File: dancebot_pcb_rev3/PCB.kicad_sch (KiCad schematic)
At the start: 30 parts, among them J1 Voltage Regulator, J10 NeoPixel Right Eye, J11 Rocker Switch, J2 IO14 servo 1, J3 IO13 servo 2, J4 IO12 servo 3, J5 IO15 servo 4, J6 IO18 servo 5 (hat), J8 Pins, J9 NeoPixel Left Eye, Q1 IRLML6402TRPBF, U1 IRLML2502TRPBF, U2 ESP32-DEVKITC-32U

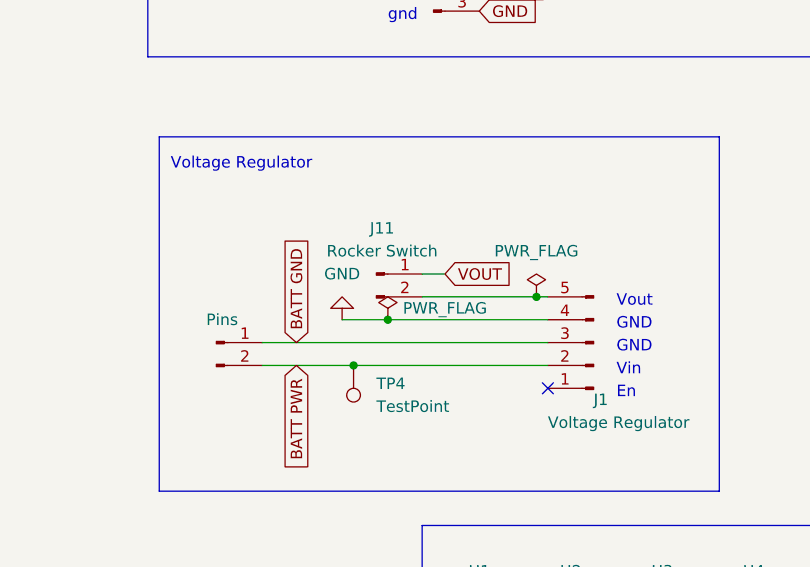
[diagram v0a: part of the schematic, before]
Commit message: changed BATT GND to GND, added some silkscreen labels
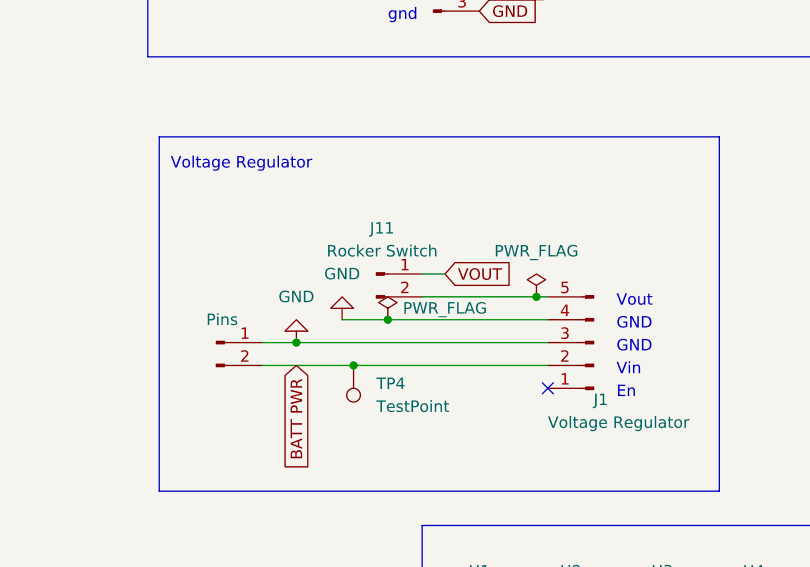
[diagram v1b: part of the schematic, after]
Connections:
- net BATT GND is gone; now on net GND: J1.3 (Pin_3), J8.1 (Pin_1)
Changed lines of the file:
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@@
   (junction (at 195.58 91.44) (diameter 0) (color 0 0 0 0)
+  )
+  (junction (at 96.52 121.92) (diameter 0) (color 0 0 0 0)
   )
   (junction (at 123.19 116.84) (diameter 0) (color 0 0 0 0)
@@
     (stroke (width 0) (type default))
   )
-  (wire (pts (xy 92.71 121.92) (xy 124.46 121.92))
+  (wire (pts (xy 92.71 121.92) (xy 96.52 121.92))
     (stroke (width 0) (type default))
   )
@@
   )
   (wire (pts (xy 101.6 119.38) (xy 106.68 119.38))
+    (stroke (width 0) (type default))
+  )
+  (wire (pts (xy 96.52 121.92) (xy 124.46 121.92))
     (stroke (width 0) (type default))
   )
@@
     (effects (font (size 1.27 1.27)) (justify left))
     (property "Intersheetrefs" "${INTERSHEET_REFS}" (at 231.948 25.4 0)
-      (effects (font (size 1.27 1.27)) (justify left) hide)
-    )
-  )
-  (global_label "BATT GND" (shape input) (at 96.52 121.92 90) (fields_autoplaced)
-    (effects (font (size 1.27 1.27)) (justify left))
-    (property "Intersheetrefs" "${INTERSHEET_REFS}" (at 96.52 109.8029 90)
       (effects (font (size 1.27 1.27)) (justify left) hide)
     )
@@
         )
       )
+    )
+  )
+  (symbol (lib_id "power:GND") (at 96.52 121.92 180) (unit 1)
+    (in_bom yes) (on_board yes) (dnp no) (fields_autoplaced)
+    (property "Reference" "#PWR04" (at 96.52 115.57 0)
+      (effects (font (size 1.27 1.27)) hide)
+    )
+    (property "Value" "GND" (at 96.52 116.84 0)
+      (effects (font (size 1.27 1.27)))
+    )
+    (property "Footprint" "" (at 96.52 121.92 0)
+      (effects (font (size 1.27 1.27)) hide)
+    )
+    (property "Datasheet" "" (at 96.52 121.92 0)
+      (effects (font (size 1.27 1.27)) hide)
+    )
+    (pin "1")
+    (instances
+      (project "PCB"
+        (path "/21324b60-e5e7-4de6-a38d-f4cdf81a1b2c"
+          (reference "#PWR04") (unit 1)
+        )
+      )

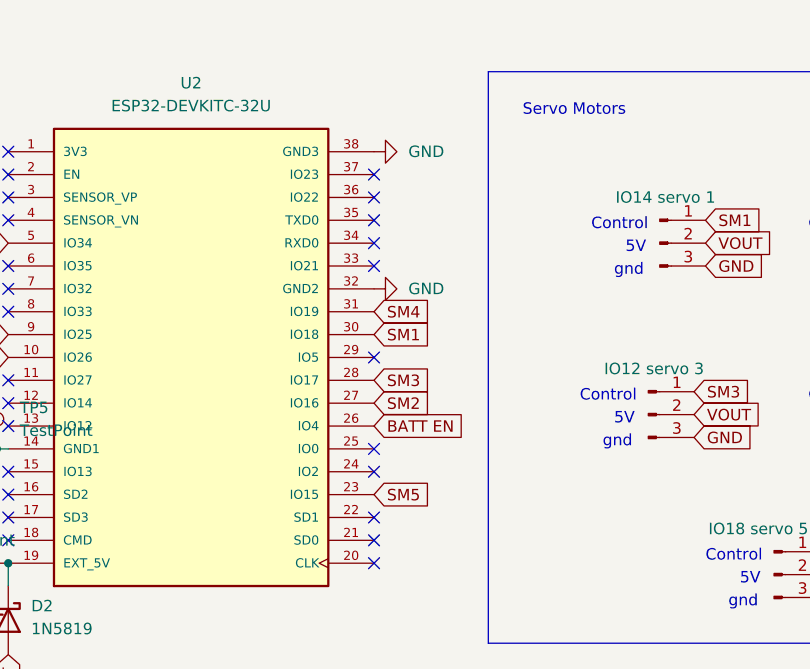
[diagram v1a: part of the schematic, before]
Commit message: shifted servo control pins to not occupy gpio15, a pin used during bootup
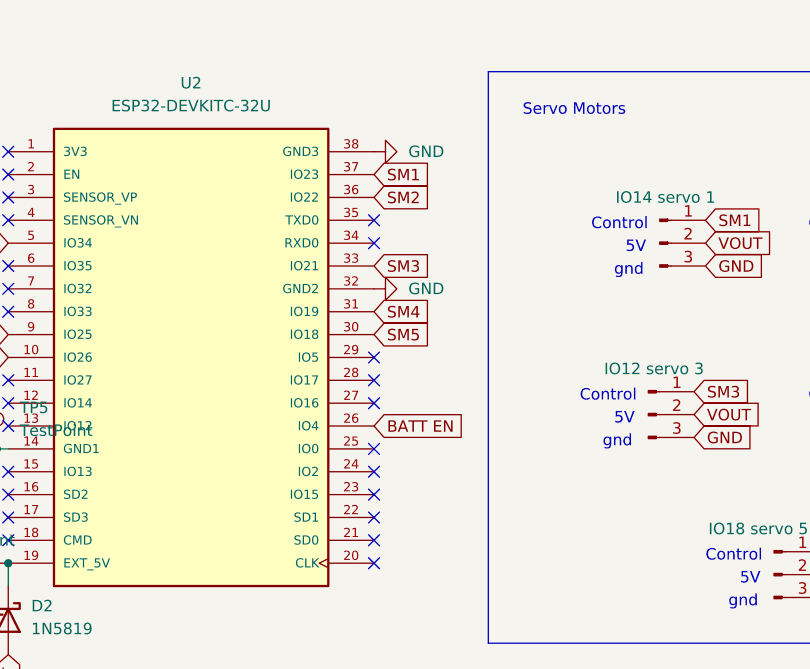
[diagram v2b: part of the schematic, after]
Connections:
- net SM1: now also U2.37 (IO23); no longer U2.30 (IO18)
- net SM2: now also U2.36 (IO22); no longer U2.27 (IO16)
- net SM3: now also U2.33 (IO21); no longer U2.28 (IO17)
- net SM5: now also U2.30 (IO18); no longer U2.23 (IO15)
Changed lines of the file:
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@@
   )
   (no_connect (at 67.31 58.42))
-  (no_connect (at 67.31 48.26))
   (no_connect (at 26.67 71.12))
   (no_connect (at 26.67 38.1))
   (no_connect (at 26.67 48.26))
   (no_connect (at 67.31 76.2))
-  (no_connect (at 67.31 38.1))
-  (no_connect (at 67.31 40.64))
   (no_connect (at 26.67 43.18))
   (no_connect (at 26.67 78.74))
@@
   (no_connect (at 170.18 129.54))
   (no_connect (at 26.67 66.04))
+  (no_connect (at 67.31 60.96))
   (no_connect (at 124.46 127))
   (no_connect (at 26.67 73.66))
+  (no_connect (at 67.31 73.66))
+  (no_connect (at 67.31 63.5))
   (no_connect (at 26.67 50.8))
   (no_connect (at 67.31 78.74))
@@
     )
   )
-  (global_label "SM3" (shape input) (at 67.31 60.96 0) (fields_autoplaced)
-    (effects (font (size 1.27 1.27)) (justify left))
-    (property "Intersheetrefs" "${INTERSHEET_REFS}" (at 74.1656 60.96 0)
-      (effects (font (size 1.27 1.27)) (justify left) hide)
-    )
-  )
   (global_label "NPLeftEye" (shape input) (at 170.18 121.92 0) (fields_autoplaced)
     (effects (font (size 1.27 1.27)) (justify left))
@@
     )
   )
+  (global_label "SM4" (shape input) (at 67.31 53.34 0) (fields_autoplaced)
+    (effects (font (size 1.27 1.27)) (justify left))
+    (property "Intersheetrefs" "${INTERSHEET_REFS}" (at 74.1656 53.34 0)
+      (effects (font (size 1.27 1.27)) (justify left) hide)
+    )
+  )
   (global_label "SM3" (shape input) (at 102.87 62.23 0) (fields_autoplaced)
     (effects (font (size 1.27 1.27)) (justify left))
@@
     )
   )
-  (global_label "SM2" (shape input) (at 67.31 63.5 0) (fields_autoplaced)
-    (effects (font (size 1.27 1.27)) (justify left))
-    (property "Intersheetrefs" "${INTERSHEET_REFS}" (at 74.1656 63.5 0)
-      (effects (font (size 1.27 1.27)) (justify left) hide)
-    )
-  )
   (global_label "VOUT" (shape input) (at 113.03 114.3 0) (fields_autoplaced)
     (effects (font (size 1.27 1.27)) (justify left))
@@
     )
   )
+  (global_label "SM3" (shape input) (at 67.31 48.26 0) (fields_autoplaced)
+    (effects (font (size 1.27 1.27)) (justify left))
+    (property "Intersheetrefs" "${INTERSHEET_REFS}" (at 74.1656 48.26 0)
+      (effects (font (size 1.27 1.27)) (justify left) hide)
+    )
+  )
   (global_label "NPLeftEye" (shape input) (at 26.67 55.88 180) (fields_autoplaced)
     (effects (font (size 1.27 1.27)) (justify right))
@@
     )
   )
-  (global_label "SM5" (shape input) (at 67.31 73.66 0) (fields_autoplaced)
-    (effects (font (size 1.27 1.27)) (justify left))
-    (property "Intersheetrefs" "${INTERSHEET_REFS}" (at 74.1656 73.66 0)
+  (global_label "SM2" (shape input) (at 67.31 40.64 0) (fields_autoplaced)
+    (effects (font (size 1.27 1.27)) (justify left))
+    (property "Intersheetrefs" "${INTERSHEET_REFS}" (at 74.1656 40.64 0)
       (effects (font (size 1.27 1.27)) (justify left) hide)
     )
@@
     )
   )
-  (global_label "SM1" (shape input) (at 67.31 55.88 0) (fields_autoplaced)
+  (global_label "SM1" (shape input) (at 67.31 38.1 0) (fields_autoplaced)
+    (effects (font (size 1.27 1.27)) (justify left))
+    (property "Intersheetrefs" "${INTERSHEET_REFS}" (at 74.1656 38.1 0)
+      (effects (font (size 1.27 1.27)) (justify left) hide)
+    )
+  )
+  (global_label "GND" (shape input) (at 128.27 48.26 0) (fields_autoplaced)
+    (effects (font (size 1.27 1.27)) (justify left))
+    (property "Intersheetrefs" "${INTERSHEET_REFS}" (at 135.1257 48.26 0)
+      (effects (font (size 1.27 1.27)) (justify left) hide)
+    )
+  )
+  (global_label "SM5" (shape input) (at 67.31 55.88 0) (fields_autoplaced)
     (effects (font (size 1.27 1.27)) (justify left))
     (property "Intersheetrefs" "${INTERSHEET_REFS}" (at 74.1656 55.88 0)
@@
     )
   )
-  (global_label "GND" (shape input) (at 128.27 48.26 0) (fields_autoplaced)
-    (effects (font (size 1.27 1.27)) (justify left))
-    (property "Intersheetrefs" "${INTERSHEET_REFS}" (at 135.1257 48.26 0)
-      (effects (font (size 1.27 1.27)) (justify left) hide)
-    )
-  )
   (global_label "VOUT" (shape input) (at 104.14 45.72 0) (fields_autoplaced)
     (effects (font (size 1.27 1.27)) (justify left))
@@
       (effects (font (size 1.27 1.27)) (justify left) hide)
     )
-  )
-  (global_label "SM4" (shape input) (at 67.31 53.34 0) (fields_autoplaced)
-    (effects (font (size 1.27 1.27)) (justify left))
-    (property "Intersheetrefs" "${INTERSHEET_REFS}" (at 74.1656 53.34 0)
-      (effects (font (size 1.27 1.27)) (justify left) hide)
-    )
